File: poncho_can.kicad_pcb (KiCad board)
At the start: 2 copper layers, 85.7 x 79.6 mm, 43 parts, among them J10 GS2, J101 DB9_Male_MountingHoles, J102 DB9_Male_MountingHoles, J103 GS2, J104 GS2, J105 GS2, J106 GS2, J7 GS2, J8 GS2, J9 GS2, U101 TJA1051T, U102 TJA1051T

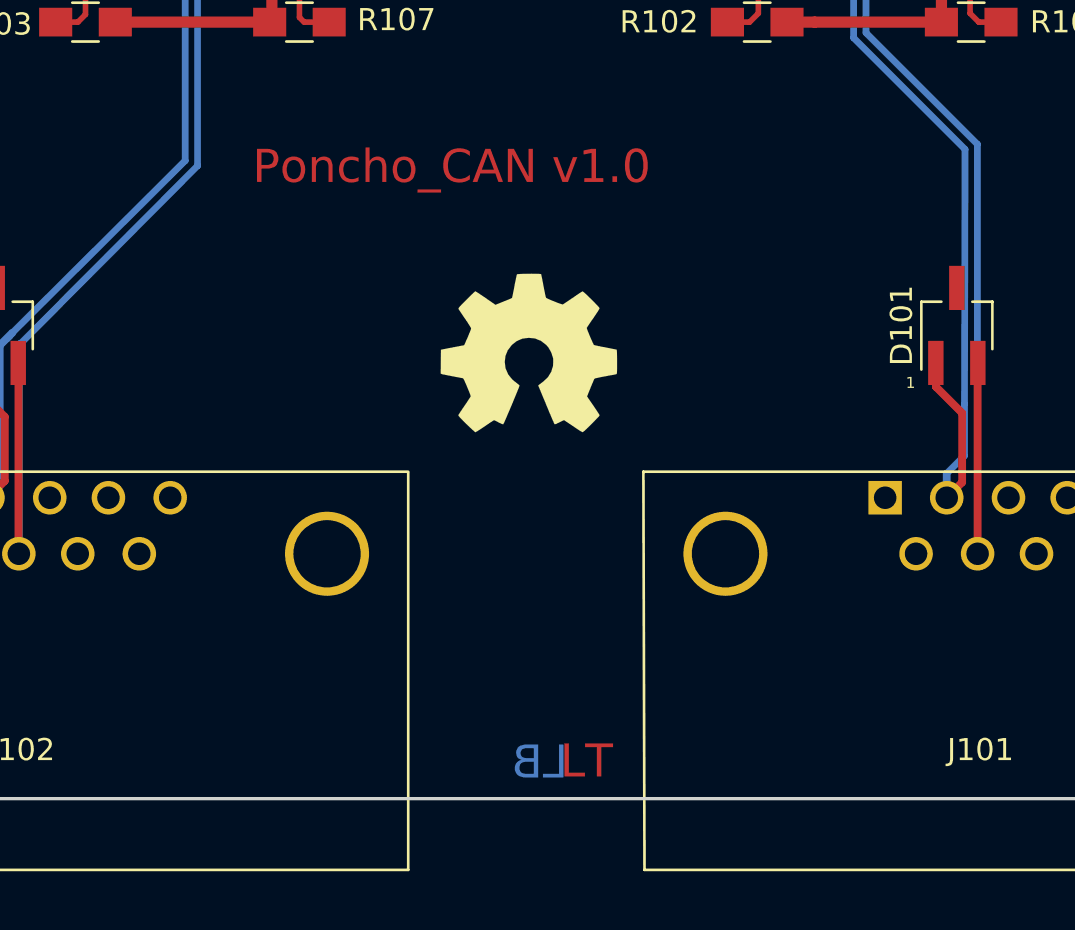
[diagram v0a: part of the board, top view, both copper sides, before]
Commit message: Agrego texto Industria Argentina, y el fill de la mascara sobre el texto
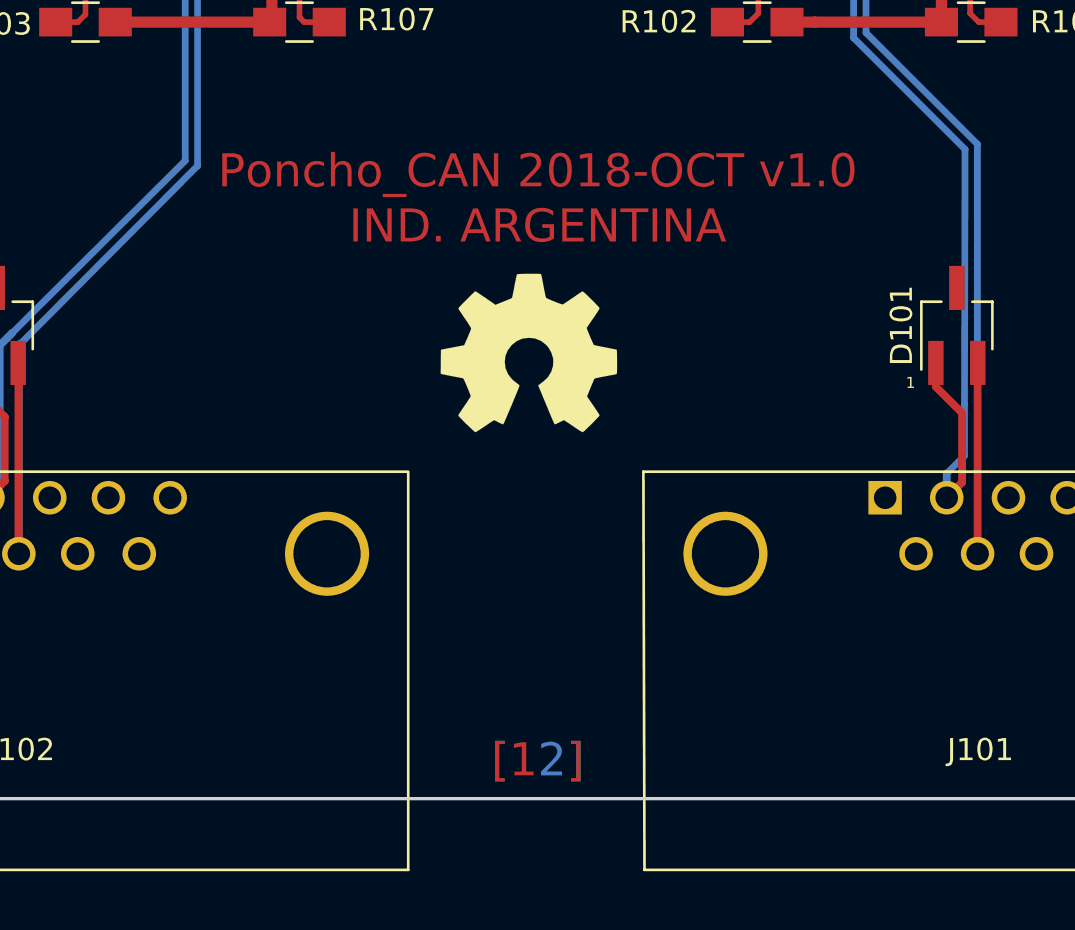
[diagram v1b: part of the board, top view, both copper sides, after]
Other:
- board text added: "Grilla 0.5mm Margen 0.25mm Vias 1mm - agujero vias 0.5mm Track mas pequeño 0.254mm (10mils)"
- board text added: "IND. ARGENTINA"
- board text added: "Poncho_CAN 2018-OCT v1.0"
- board text added: "[ 2]"
- board text added: "[1 ]"
- board text removed: "Grilla 0.1mm Clearence 0.25mm Vias 1mm - agujero vias 0.5mm Track mas pequeño 0.254mm (10mils)"
- board text removed: "LB"
- board text removed: "LT"
- board text removed: "Poncho_CAN v1.0"
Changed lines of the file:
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@@
   (general
     (links 90)
-    (no_connects 32)
-    (area 17.572141 15.774999 279.500001 146.235001)
+    (no_connects 0)
+    (area 65.724999 54.319999 151.575001 134.025001)
     (thickness 1.6)
-    (drawings 27)
+    (drawings 30)
     (tracks 206)
     (zones 0)
@@
     )
   )
+  (dimension 85.700015 (width 0.3) (layer Dwgs.User)
+    (gr_text "85,700 mm" (at 108.662922 156.074992 0.03342810561) (layer Dwgs.User)
+      (effects (font (size 1.5 1.5) (thickness 0.3)))
+    )
+    (feature1 (pts (xy 65.8 133.95) (xy 65.81371 157.449992)))
+    (feature2 (pts (xy 151.5 133.9) (xy 151.51371 157.399992)))
+    (crossbar (pts (xy 151.512135 154.699992) (xy 65.812135 154.749992)))
+    (arrow1a (pts (xy 65.812135 154.749992) (xy 66.938296 154.162914)))
+    (arrow1b (pts (xy 65.812135 154.749992) (xy 66.938981 155.335755)))
+    (arrow2a (pts (xy 151.512135 154.699992) (xy 150.385289 154.114229)))
+    (arrow2b (pts (xy 151.512135 154.699992) (xy 150.385974 155.28707)))
+  )
+  (dimension 79.5 (width 0.3) (layer Dwgs.User)
+    (gr_text "79,500 mm" (at 161.15 94.15 270) (layer Dwgs.User)
+      (effects (font (size 1.5 1.5) (thickness 0.3)))
+    )
+    (feature1 (pts (xy 151.5 133.9) (xy 162.5 133.9)))
+    (feature2 (pts (xy 151.5 54.4) (xy 162.5 54.4)))
+    (crossbar (pts (xy 159.8 54.4) (xy 159.8 133.9)))
+    (arrow1a (pts (xy 159.8 133.9) (xy 159.213579 132.773496)))
+    (arrow1b (pts (xy 159.8 133.9) (xy 160.386421 132.773496)))
+    (arrow2a (pts (xy 159.8 54.4) (xy 159.213579 55.526504)))
+    (arrow2b (pts (xy 159.8 54.4) (xy 160.386421 55.526504)))
+  )
+  (gr_text "IND. ARGENTINA" (at 109 108) (layer F.Cu)
+    (effects (font (size 1.5 1.5) (thickness 0.3)))
+  )
   (gr_text 1 (at 125.9 115.1) (layer F.SilkS)
     (effects (font (size 0.5 0.5) (thickness 0.1)))
@@
   (gr_line (start 84.3 69.5) (end 84.3 71) (layer F.SilkS) (width 0.2))
   (gr_line (start 133.2 69.5) (end 133.2 71) (layer F.SilkS) (width 0.2))
-  (gr_text "Poncho_CAN v1.0" (at 105.1 105.3) (layer F.Cu)
+  (gr_text "Poncho_CAN 2018-OCT v1.0" (at 109 105.5) (layer F.Cu)
     (effects (font (size 1.5 1.5) (thickness 0.3)))
   )
-  (gr_text "Grilla 0.1mm\nClearence 0.25mm\nVias 1mm - agujero vias 0.5mm\nTrack mas pequeño 0.254mm (10mils)" (at 19 37.8) (layer Dwgs.User)
+  (gr_text "Grilla 0.5mm\nMargen 0.25mm\nVias 1mm - agujero vias 0.5mm\nTrack mas pequeño 0.254mm (10mils)" (at 19 37.8) (layer Dwgs.User)
     (effects (font (size 1.5 1.5) (thickness 0.3)) (justify left))
   )
-  (gr_text "    LB" (at 110.4 132.3) (layer B.Cu)
-    (effects (font (size 1.5 1.5) (thickness 0.3)) (justify mirror))
-  )
-  (gr_text "    LT" (at 109.9 132.25) (layer F.Cu)
+  (gr_text "[  2]" (at 109 132.2) (layer B.Cu)
+    (effects (font (size 1.5 1.5) (thickness 0.3)))
+  )
+  (gr_text "[1  ]" (at 109 132.2) (layer F.Cu)
     (effects (font (size 1.5 1.5) (thickness 0.3)))
   )
@@
   (segment (start 128.34579 116.068799) (end 128.371201 104.516331) (width 0.3048) (layer B.Cu) (net 25))
   (segment (start 122.1 91.25) (end 122.973 90.377) (width 0.508) (layer F.Cu) (net 25))
+  (segment (start 118.74 91.25) (end 121.173 91.25) (width 0.508) (layer F.Cu) (net 25))
+  (segment (start 121.173 91.25) (end 122.1 91.25) (width 0.508) (layer F.Cu) (net 25))
   (segment (start 122.973 90.377) (end 122.973 89.25) (width 0.508) (layer F.Cu) (net 25))
-  (segment (start 121.173 91.25) (end 122.1 91.25) (width 0.508) (layer F.Cu) (net 25))
   (segment (start 123.320601 99.465727) (end 123.320601 89.597601) (width 0.3048) (layer B.Cu) (net 25))
   (via (at 122.973 89.25) (size 1) (drill 0.5) (layers F.Cu B.Cu) (net 25))
   (segment (start 128.371201 104.516331) (end 123.320601 99.465727) (width 0.3048) (layer B.Cu) (net 25))
   (segment (start 123.320601 89.597601) (end 122.973 89.25) (width 0.3048) (layer B.Cu) (net 25))
-  (segment (start 118.74 91.25) (end 121.173 91.25) (width 0.508) (layer F.Cu) (net 25))
   (segment (start 93.579399 105.265729) (end 85.547961 113.33309) (width 0.3048) (layer B.Cu) (net 26))
   (segment (start 85.547961 113.33309) (end 85.53 113.31513) (width 0.3048) (layer B.Cu) (net 26))
@@
       )
     )
+  )
+  (zone (net 2) (net_name GND) (layer F.Mask) (hatch edge 0.508)
+    (connect_pads (clearance 0.2032))
+    (min_thickness 0.254)
+    (fill yes (arc_segments 16) (thermal_gap 0.508) (thermal_bridge_width 0.508))
+    (polygon
+      (pts
+        (xy 125.5 104) (xy 125.5 107) (xy 92.5 107) (xy 92.5 104)
+      )
+    )
+  )
+  (zone (net 2) (net_name GND) (layer F.Mask) (hatch edge 0.508)
+    (connect_pads (clearance 0.2032))
+    (min_thickness 0.254)
+    (fill yes (arc_segments 16) (thermal_gap 0.508) (thermal_bridge_width 0.508))
+    (polygon
+      (pts
+        (xy 118 107) (xy 118 109.5) (xy 100 109.5) (xy 100 107)
+      )
+    )

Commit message: Agrego al ruta 3D de un resistor que me faltó
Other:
- board text added: "Grilla 0.1mm Margen 0.25mm Vias 1mm - agujero vias 0.5mm Track mas pequeño 0.254mm (10mils)"
- board text removed: "Grilla 0.5mm Margen 0.25mm Vias 1mm - agujero vias 0.5mm Track mas pequeño 0.254mm (10mils)"
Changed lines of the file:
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@@
     (pad 2 smd rect (at 1.35 0 180) (size 1.5 1.3) (layers F.Cu F.Paste F.Mask)
       (net 19 "Net-(J106-Pad1)"))
-    (model ${KISYS3DMOD}/Resistors_SMD.3dshapes/R_0805.wrl
+    (model ${KIPRJMOD}/shapes3D/R_0805.wrl
       (at (xyz 0 0 0))
       (scale (xyz 1 1 1))
@@
     (effects (font (size 1.5 1.5) (thickness 0.3)))
   )
-  (gr_text "Grilla 0.5mm\nMargen 0.25mm\nVias 1mm - agujero vias 0.5mm\nTrack mas pequeño 0.254mm (10mils)" (at 19 37.8) (layer Dwgs.User)
+  (gr_text "Grilla 0.1mm\nMargen 0.25mm\nVias 1mm - agujero vias 0.5mm\nTrack mas pequeño 0.254mm (10mils)" (at 19 37.8) (layer Dwgs.User)
     (effects (font (size 1.5 1.5) (thickness 0.3)) (justify left))
   )

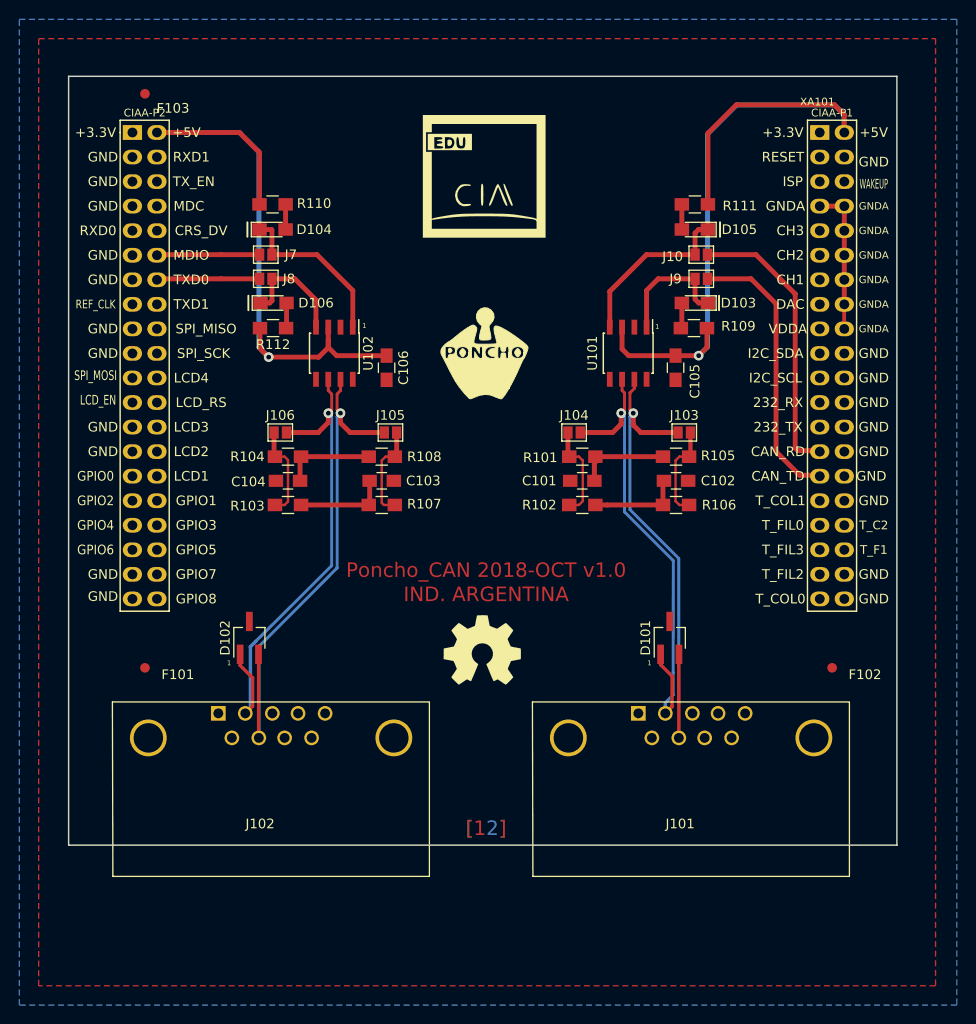
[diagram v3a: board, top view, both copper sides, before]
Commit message: Multiples correcciones:
- Se removió segunda licencia en la raiz
- Se corrigió licencia en doc/licencia
- Se agrego la información de la licencia al rótulo del esquemático y pcb
- Se escondieron las serigrafias de los fiduciarios
- Se movio la serigrafia de J101 y J102
- Se agregó la información del fabricante
- Se agregó la información de la terminación
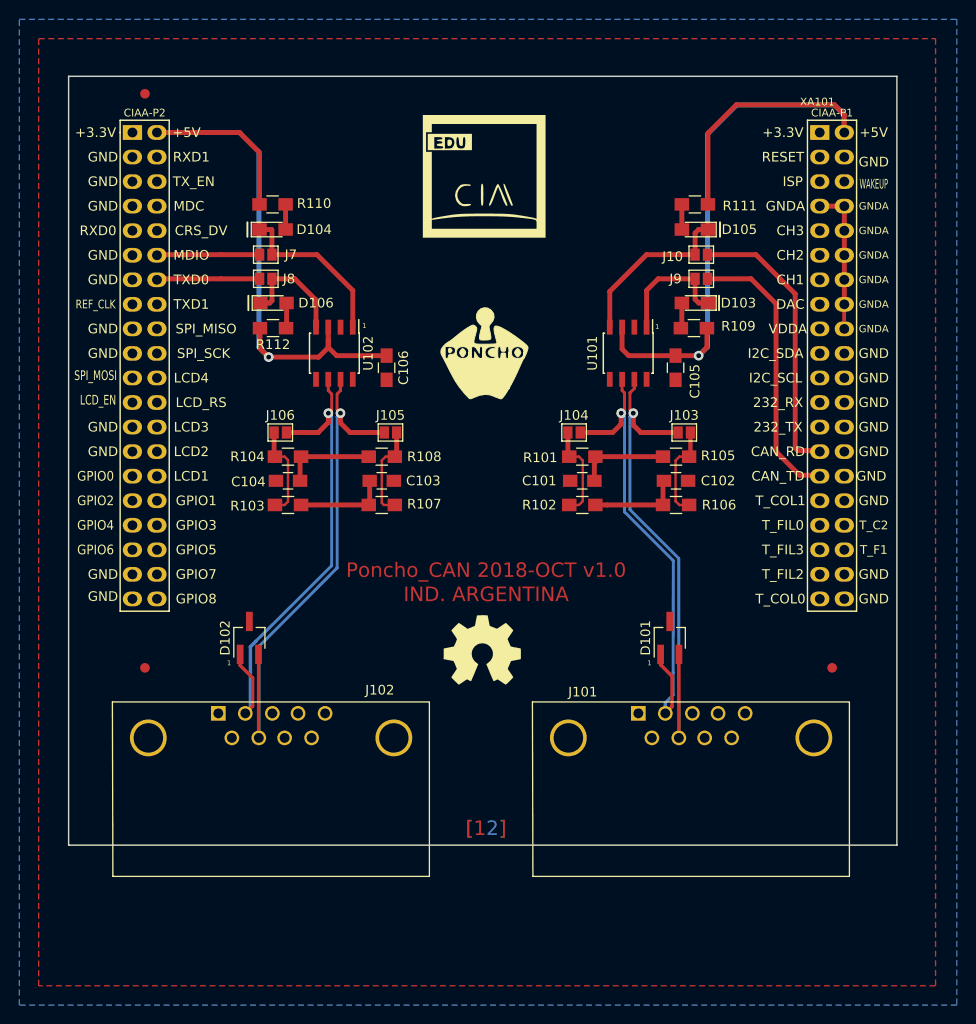
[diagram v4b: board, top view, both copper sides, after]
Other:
- board text added: "Mínimos (Mayer 10mils): Grilla 0.1mm Margen 0.25mm Vias 1mm - agujero vias 0.5mm Track mas pequeño 0.254mm (10mils) Terminación: HASL"
- board text removed: "Grilla 0.1mm Margen 0.25mm Vias 1mm - agujero vias 0.5mm Track mas pequeño 0.254mm (10mils)"
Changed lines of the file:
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@@
     (company "Proyecto CIAA - COMPUTADORA INDUSTRIAL ABIERTA ARGENTINA")
     (comment 1 https://github.com/ggavinowich/CESE_PCB_poncho_CAN)
-    (comment 2 "Gabriel Gavinowich - Licencia MIT")
-    (comment 3 "Autor Gabriel Gavinowich")
+    (comment 2 "Licencia: Ver doc/LICENCIA.txt")
+    (comment 3 "Autor: Gabriel Gavinowich")
   )
   (layers
@@
     (descr "Connecteur DB9 male couche")
     (tags "CONN DB9")
-    (fp_text reference J101 (at -4.32 -11.43 180) (layer F.SilkS)
+    (fp_text reference J101 (at 5.75 2.21 180) (layer F.SilkS)
       (effects (font (size 1 1) (thickness 0.15)))
     )
@@
     (descr "Connecteur DB9 male couche")
     (tags "CONN DB9")
-    (fp_text reference J102 (at -4.32 -11.43 180) (layer F.SilkS)
+    (fp_text reference J102 (at -16.71 2.41 180) (layer F.SilkS)
       (effects (font (size 1 1) (thickness 0.15)))
     )
@@
     (tags marker)
     (attr virtual)
-    (fp_text reference F101 (at 3.4 0.7) (layer F.SilkS)
+    (fp_text reference F101 (at 3.4 0.7) (layer F.SilkS) hide
       (effects (font (size 1 1) (thickness 0.15)))
     )
@@
     (tags marker)
     (attr virtual)
-    (fp_text reference F102 (at 3.4 0.7) (layer F.SilkS)
+    (fp_text reference F102 (at 3.4 0.7) (layer F.SilkS) hide
       (effects (font (size 1 1) (thickness 0.15)))
     )
@@
     (tags marker)
     (attr virtual)
-    (fp_text reference F103 (at 2.9 1.5) (layer F.SilkS)
+    (fp_text reference F103 (at -3.1 0) (layer F.SilkS) hide
       (effects (font (size 1 1) (thickness 0.15)))
     )
@@
     (effects (font (size 1.5 1.5) (thickness 0.3)))
   )
-  (gr_text "Grilla 0.1mm\nMargen 0.25mm\nVias 1mm - agujero vias 0.5mm\nTrack mas pequeño 0.254mm (10mils)" (at 19 37.8) (layer Dwgs.User)
+  (gr_text "Mínimos (Mayer 10mils):\nGrilla 0.1mm\nMargen 0.25mm\nVias 1mm - agujero vias 0.5mm\nTrack mas pequeño 0.254mm (10mils)\nTerminación: HASL" (at 19 37.8) (layer Dwgs.User)
     (effects (font (size 1.5 1.5) (thickness 0.3)) (justify left))
   )
